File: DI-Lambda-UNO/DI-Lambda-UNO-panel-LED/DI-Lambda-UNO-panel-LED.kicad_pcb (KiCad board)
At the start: 2 copper layers, 33.2 x 26.6 mm, 6 parts, among them J1 Conn_01X06, U1 24LC02

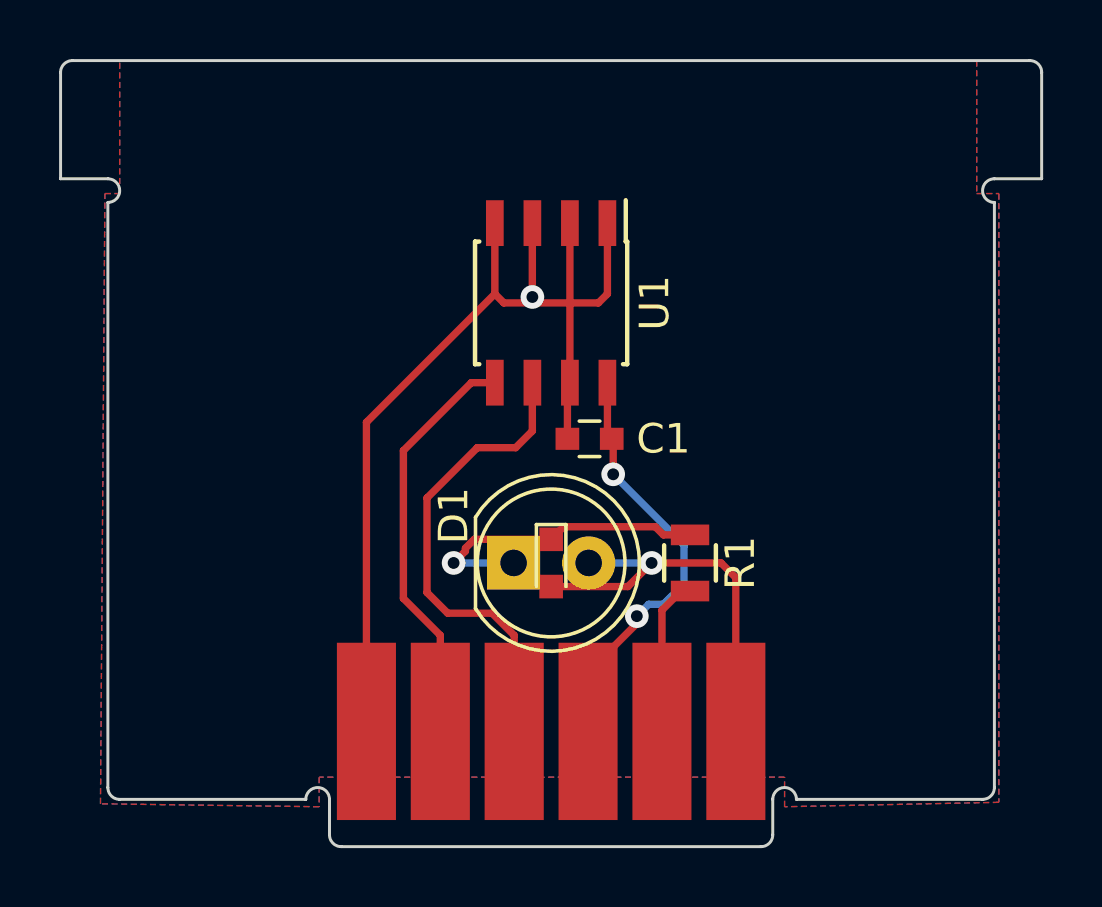
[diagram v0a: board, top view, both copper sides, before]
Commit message: LED board: convert to 18mm height
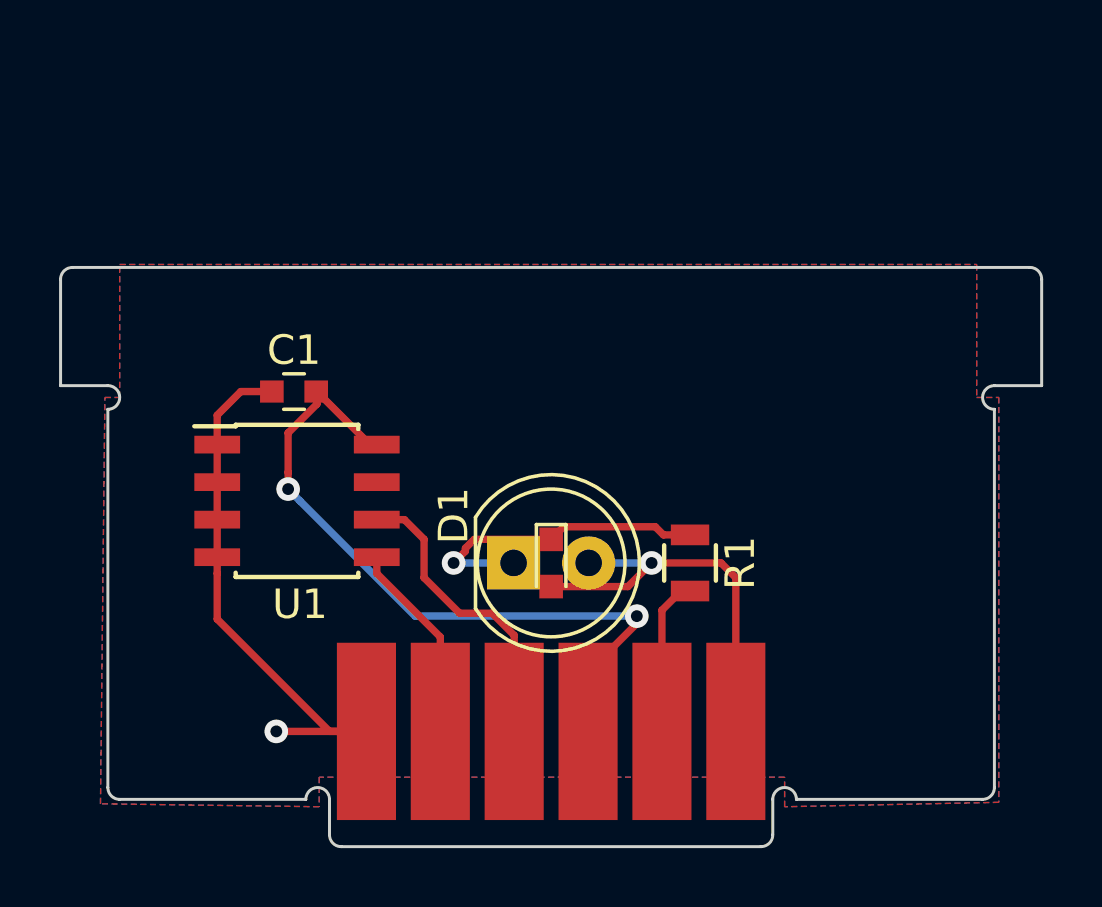
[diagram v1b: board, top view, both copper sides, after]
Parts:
- moved U1 10.9 mm to (151.4, 81.9), turned to 0 degrees
- moved C1 10.1 mm to (151.3, 78.2)
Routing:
- net GND: track 34.1 -> 18.8 mm
- net /VCC: track 13.0 -> 23.2 mm
- net /SCL: track 14.6 -> 8.78 mm
- net /SDA: track 12.6 -> 6.79 mm
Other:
- board size 33.2 x 26.6 mm -> 33.2 x 19.6 mm
- board text added: "DI-Lambda UNO v1.3"
- board text removed: "DI-Lambda UNO v1.1"

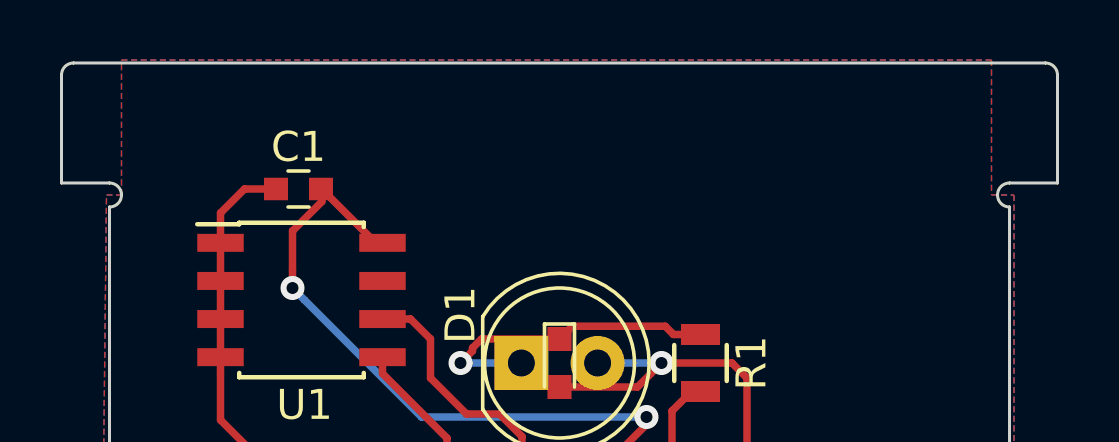
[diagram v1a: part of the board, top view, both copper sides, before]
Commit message: Update schematics to version 1.3
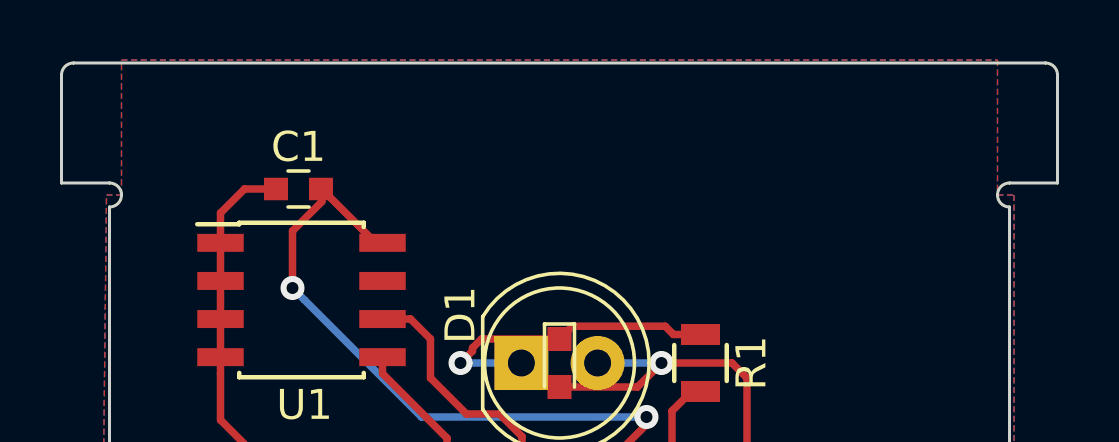
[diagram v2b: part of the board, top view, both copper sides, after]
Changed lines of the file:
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@@
     (visible_elements FFFFEF7F)
     (pcbplotparams
-      (layerselection 0x000f0_ffffffff)
+      (layerselection 0x010f0_ffffffff)
       (usegerberextensions true)
       (usegerberattributes true)
@@
       (drillshape 0)
       (scaleselection 1)
-      (outputdirectory DI-Lambda-UNO-panel-LED-v1.0-gerbers-20170824/))
+      (outputdirectory DI-Lambda-UNO-panel-LED-v1.3-gerbers-2017dec10))
   )
   (net 0 "")
@@
     (polygon
       (pts
-        (xy 145.4 73.9) (xy 174.4 73.9) (xy 174.4 78.4) (xy 175.15 78.4) (xy 175.15 92.1)
+        (xy 145.4 73.9) (xy 174.6 73.9) (xy 174.6 78.4) (xy 175.15 78.4) (xy 175.15 92.1)
         (xy 167.9 92.25) (xy 167.9 91.25) (xy 152.15 91.25) (xy 152.15 92.25) (xy 144.75 92.15)
         (xy 144.9 78.4) (xy 145.4 78.4)
@@
     (polygon
       (pts
-        (xy 145.4 73.9) (xy 174.4 73.9) (xy 174.4 78.4) (xy 175.15 78.4) (xy 175.15 92.1)
+        (xy 145.4 73.9) (xy 174.6 73.9) (xy 174.6 78.4) (xy 175.15 78.4) (xy 175.15 92.1)
         (xy 167.9 92.25) (xy 167.9 91.25) (xy 152.15 91.25) (xy 152.15 92.25) (xy 144.75 92.15)
         (xy 144.9 78.4) (xy 145.4 78.4)

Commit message: Version 1.5
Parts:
- added MK1: Mounting_Hole, DI-Lambda-module-tabs:Tab_LED, F.Cu at (160.0, 92.0)
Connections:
- J1 pad 1: GND -> /VCC
- J1 pad 4: /VCC -> GND
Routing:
- net /VCC: track 23.2 -> 15.6 mm, vias 2 -> 0
- net GND: track 18.8 -> 12.0 mm, vias 1 -> 2
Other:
- board size 33.2 x 19.6 mm -> 33.2 x 25 mm
- board text added: "DI-Lambda UNO v1.5"
- board text removed: "DI-Lambda UNO v1.3"

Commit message: Version 1.6
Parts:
- added R2: 4.7K, Resistor_SMD:R_0603_1608Metric, F.Cu at (155.0, 78.2)
- added W1: WRITE, TestPoint:TestPoint_Pad_D2.5mm, F.Cu at (151.3, 73.8)
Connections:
- U1 pad 7: GND -> Net-(R2-Pad2)
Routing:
- net Net-(R2-Pad2): track 0.00 -> 12.6 mm
- net /VCC: track 15.6 -> 17.0 mm
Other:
- board text added: "DI-Lambda UNO v1.6"
- board text added: "Write"
- board text removed: "DI-Lambda UNO v1.5"
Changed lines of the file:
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@@
   (general
     (thickness 1.6)
-    (drawings 19)
-    (tracks 47)
+    (drawings 20)
+    (tracks 54)
     (zones 0)
-    (modules 7)
-    (nets 8)
+    (modules 9)
+    (nets 9)
   )
   (page A4)
@@
       (psa4output false)
       (plotreference true)
-      (plotvalue true)
+      (plotvalue false)
       (plotinvisibletext false)
       (padsonsilk false)
@@
       (drillshape 0)
       (scaleselection 1)
-      (outputdirectory DI-Lambda-UNO-panel-LED-v1.5-gerbers-2018feb07-1))
+      (outputdirectory DI-Lambda-UNO-panel-LED-v1.6-gerbers-2018-mar-26))
   )
   (net 0 "")
@@
   (net 6 /VLED)
   (net 7 "Net-(D1-Pad1)")
+  (net 8 "Net-(R2-Pad2)")
   (net_class Default "This is the default net class."
     (clearance 0.2)
@@
     (add_net GND)
     (add_net "Net-(D1-Pad1)")
+    (add_net "Net-(R2-Pad2)")
+  )
+  (module Resistor_SMD:R_0603_1608Metric (layer F.Cu)
+    (at 154.975 78.2)
+    (descr "Resistor SMD 0603 (1608 Metric), square (rectangular) end terminal, IPC_7351 nominal, (Body size source: http://www.tortai-tech.com/upload/download/2011102023233369053.pdf), generated with kicad-footprint-generator")
+    (tags resistor)
+    (attr smd)
+    (fp_text reference R2 (at -0.475 -1.35) (layer F.SilkS)
+      (effects (font (size 1 1) (thickness 0.15)))
+    )
+    (fp_text value 4.7K (at 0 1.65) (layer F.Fab)
+      (effects (font (size 1 1) (thickness 0.15)))
+    )
+    (fp_line (start -0.8 0.4) (end -0.8 -0.4) (layer F.Fab) (width 0.1))
+    (fp_line (start -0.8 -0.4) (end 0.8 -0.4) (layer F.Fab) (width 0.1))
+    (fp_line (start 0.8 -0.4) (end 0.8 0.4) (layer F.Fab) (width 0.1))
+    (fp_line (start 0.8 0.4) (end -0.8 0.4) (layer F.Fab) (width 0.1))
+    (fp_line (start -0.22 -0.51) (end 0.22 -0.51) (layer F.SilkS) (width 0.12))
+    (fp_line (start -0.22 0.51) (end 0.22 0.51) (layer F.SilkS) (width 0.12))
+    (fp_line (start -1.46 0.75) (end -1.46 -0.75) (layer F.CrtYd) (width 0.05))
+    (fp_line (start -1.46 -0.75) (end 1.46 -0.75) (layer F.CrtYd) (width 0.05))
+    (fp_line (start 1.46 -0.75) (end 1.46 0.75) (layer F.CrtYd) (width 0.05))
+    (fp_line (start 1.46 0.75) (end -1.46 0.75) (layer F.CrtYd) (width 0.05))
+    (fp_text user %R (at 0 0) (layer F.Fab)
+      (effects (font (size 0.5 0.5) (thickness 0.08)))
+    )
+    (pad 1 smd rect (at -0.875 0) (size 0.67 1) (layers F.Cu F.Paste F.Mask)
+      (net 4 /VCC))
+    (pad 2 smd rect (at 0.875 0) (size 0.67 1) (layers F.Cu F.Paste F.Mask)
+      (net 8 "Net-(R2-Pad2)"))
+    (model ${KISYS3DMOD}/Resistor_SMD.3dshapes/R_0603_1608Metric.wrl
+      (at (xyz 0 0 0))
+      (scale (xyz 1 1 1))
+      (rotate (xyz 0 0 0))
+    )
+  )
+  (module TestPoint:TestPoint_Pad_D2.5mm (layer F.Cu)
+    (at 151.3 73.85)
+    (descr "SMD pad as test Point, diameter 2.5mm")
+    (tags "test point SMD pad")
+    (attr virtual)
+    (fp_text reference W1 (at -2.8 -1.75) (layer F.SilkS) hide
+      (effects (font (size 1 1) (thickness 0.15)))
+    )
+    (fp_text value WRITE (at 0 2.25) (layer F.Fab)
+      (effects (font (size 1 1) (thickness 0.15)))
+    )
+    (fp_text user %R (at 0 -2.15) (layer F.Fab)
+      (effects (font (size 1 1) (thickness 0.15)))
+    )
+    (fp_circle (center 0 0) (end 1.75 0) (layer F.CrtYd) (width 0.05))
+    (fp_circle (center 0 0) (end 0 1.45) (layer F.SilkS) (width 0.12))
+    (pad 1 smd circle (at 0 0) (size 2.5 2.5) (layers F.Cu F.Mask)
+      (net 8 "Net-(R2-Pad2)"))
   )
   (module DI-Lambda-module-tabs:Tab_LED (layer F.Cu)
@@
       (net 4 /VCC))
     (pad 7 smd rect (at 2.7 -0.635) (size 1.55 0.6) (layers F.Cu F.Paste F.Mask)
-      (net 1 GND))
+      (net 8 "Net-(R2-Pad2)"))
     (pad 6 smd rect (at 2.7 0.635) (size 1.55 0.6) (layers F.Cu F.Paste F.Mask)
       (net 3 /SCL))
@@
     )
   )
-  (gr_text "DI-Lambda UNO v1.5" (at 160.45 68.65) (layer B.Mask)
+  (gr_text Write (at 151.25 71.45) (layer F.SilkS)
+    (effects (font (size 1 1) (thickness 0.2)))
+  )
+  (gr_text "DI-Lambda UNO v1.6" (at 160.45 68.65) (layer B.Mask)
     (effects (font (size 1.5 1.5) (thickness 0.3)) (justify mirror))
   )
@@
   (segment (start 155.7 83.2) (end 155.035 82.535) (width 0.25) (layer F.Cu) (net 3))
   (segment (start 155.035 82.535) (end 154.1 82.535) (width 0.25) (layer F.Cu) (net 3))
-  (segment (start 151.300004 86.250004) (end 151.300004 79.949996) (width 0.25) (layer F.Cu) (net 4))
-  (segment (start 153.75 88.7) (end 151.300004 86.250004) (width 0.25) (layer F.Cu) (net 4))
-  (segment (start 151.300004 79.949996) (end 152.075 79.175) (width 0.25) (layer F.Cu) (net 4))
   (segment (start 153.75 89.7) (end 153.75 88.7) (width 0.25) (layer F.Cu) (net 4))
   (segment (start 152.075 79.175) (end 152.075 78.2) (width 0.25) (layer F.Cu) (net 4))
+  (segment (start 153.75 88.7) (end 152.075 87.025) (width 0.25) (layer F.Cu) (net 4))
+  (segment (start 152.075 87.025) (end 152.075 79.175) (width 0.25) (layer F.Cu) (net 4))
+  (segment (start 154.1 78.2) (end 152.05 78.2) (width 0.25) (layer F.Cu) (net 4))
   (segment (start 152.05 78.2) (end 152.075 78.2) (width 0.25) (layer F.Cu) (net 4))
   (segment (start 152.075 78.2) (end 153.87 79.995) (width 0.25) (layer F.Cu) (net 4))
@@
   (segment (start 163.75 85.6) (end 164.4 84.95) (width 0.25) (layer F.Cu) (net 5))
   (segment (start 164.4 84.95) (end 164.7 84.95) (width 0.25) (layer F.Cu) (net 5))
+  (segment (start 160 84.8) (end 160.5 85.3) (width 0.25) (layer F.Cu) (net 6))
+  (segment (start 160.5 85.3) (end 162.1 85.3) (width 0.25) (layer F.Cu) (net 6))
+  (segment (start 162.1 85.3) (end 163.4 84) (width 0.25) (layer F.Cu) (net 6))
   (segment (start 163.4 84) (end 165.75 84) (width 0.25) (layer F.Cu) (net 6))
   (segment (start 165.75 84) (end 166.25 84.5) (width 0.25) (layer F.Cu) (net 6))
   (segment (start 166.25 84.5) (end 166.25 88.2) (width 0.25) (layer F.Cu) (net 6))
-  (segment (start 160 84.8) (end 162.6 84.8) (width 0.25) (layer F.Cu) (net 6))
-  (segment (start 162.6 84.8) (end 163.4 84) (width 0.25) (layer F.Cu) (net 6))
   (segment (start 161.27 84) (end 163.4 84) (width 0.25) (layer B.Cu) (net 6))
   (via (at 163.4 84) (size 0.8) (drill 0.4) (layers F.Cu B.Cu) (net 6))
@@
   (segment (start 158.73 84) (end 156.7 84) (width 0.25) (layer B.Cu) (net 7))
   (via (at 156.7 84) (size 0.8) (drill 0.4) (layers F.Cu B.Cu) (net 7))
+  (segment (start 155.85 78.2) (end 155.85 75.1) (width 0.25) (layer F.Cu) (net 8))
+  (segment (start 155.85 75.1) (end 154.6 73.85) (width 0.25) (layer F.Cu) (net 8))
+  (segment (start 154.6 73.85) (end 151.3 73.85) (width 0.25) (layer F.Cu) (net 8))
+  (segment (start 155.85 78.2) (end 155.85 80.65) (width 0.25) (layer F.Cu) (net 8))
+  (segment (start 155.85 80.65) (end 155.235 81.265) (width 0.25) (layer F.Cu) (net 8))
+  (segment (start 155.235 81.265) (end 154.1 81.265) (width 0.25) (layer F.Cu) (net 8))
   (zone (net 1) (net_name GND) (layer B.Cu) (hatch edge 0.508)
     (connect_pads (clearance 0.508))

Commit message: More missing fotprints
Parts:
- R601: renamed from R2; value 4.7K -> 4.75K
- R602: renamed from R1; value R_Small -> 470R
- moved C601 158.3 mm to (7.90, 11.2)
- moved D602 158.3 mm to (16.6, 17.0)
- moved J601 158.3 mm to (16.6, 23.7)
- moved MK601 158.3 mm to (16.6, 25.0)
- moved R601 158.3 mm to (11.6, 11.2)
- moved U601 158.3 mm to (8.00, 14.9)
- moved W601 158.3 mm to (7.90, 6.85)
- moved D601 158.3 mm to (15.3, 17.0)
- moved R602 158.3 mm to (21.3, 17.0)
- renumbered C1 to C601, D1 to D601, D2 to D602, J1 to J601, MK1 to MK601, U1 to U601, W1 to W601
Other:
- outline, holes or cut-outs redrawn
- board text added: "DI-Lambda UNO v1.7"
- board text removed: "DI-Lambda UNO v1.6"
